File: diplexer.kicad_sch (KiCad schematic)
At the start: 10 parts, among them P25 MMCX-J-P-H-ST-TH1, P26 CONUFL001-SMD-T

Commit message: Change MMCX connectors to right angle
There's not enough room on the board for vertical ones.

Signed-off-by: Corey Minyard <corey@minyard.net>
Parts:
- P25: value MMCX-J-P-H-ST-TH1 -> MMCX-J-P-H-RA-TH1; footprint PacSatDev_misc:COAX4_MMCX-J-P-H-ST-TH1_SAI -> PacSatDev_misc:COAX4_MMCX-J-P-H-RA-TH1_SAI; symbol PACSAT_DEV_misc:MMCX-J-P-H-ST-TH1 -> PACSAT_DEV_misc:MMCX-J-P-H-RA-TH1; now in the parts list
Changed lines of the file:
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@@
 	)
 	(symbol
-		(lib_id "PACSAT_DEV_misc:MMCX-J-P-H-ST-TH1")
+		(lib_id "PACSAT_DEV_misc:MMCX-J-P-H-RA-TH1")
 		(at 133.35 109.22 0)
 		(unit 1)
 		(exclude_from_sim no)
-		(in_bom no)
+		(in_bom yes)
 		(on_board yes)
 		(dnp yes)
@@
 			)
 		)
-		(property "Value" "MMCX-J-P-H-ST-TH1"
+		(property "Value" "MMCX-J-P-H-RA-TH1"
 			(at 133.35 109.22 0)
 			(effects
@@
 			)
 		)
-		(property "Footprint" "PacSatDev_misc:COAX4_MMCX-J-P-H-ST-TH1_SAI"
+		(property "Footprint" "PacSatDev_misc:COAX4_MMCX-J-P-H-RA-TH1_SAI"
 			(at 133.35 109.22 0)
 			(effects
@@
 			)
 		)
-		(property "Datasheet" "MMCX-J-P-H-ST-TH1"
+		(property "Datasheet" "MMCX-J-P-H-RA-TH1"
 			(at 133.35 109.22 0)
 			(effects

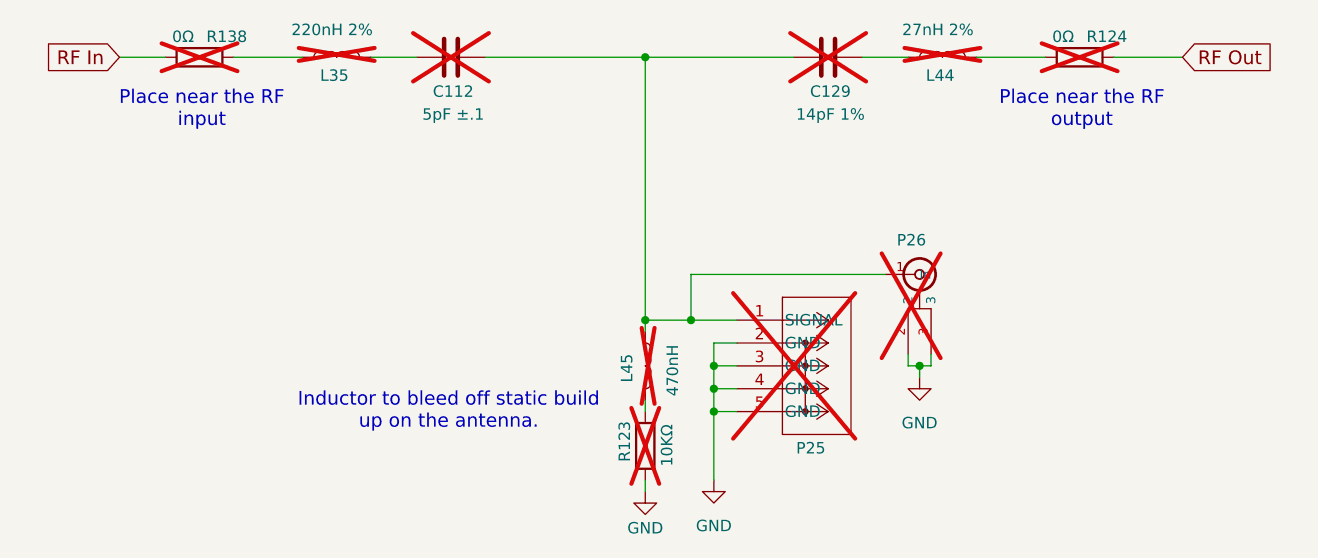
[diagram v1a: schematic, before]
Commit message: Fix issues with the RF connectors
Remove the U.FL connectors P23, P24, and P26 they just weren't going
to work and there's no good place to put them, and where they were was
shorting the MMCX connectors.  Just use the MMCX ones for output.

Move the diplexer MMCX connector to give it more room and get it a
little more out of the way of the transmit connector.

Signed-off-by: Corey Minyard <corey@minyard.net>
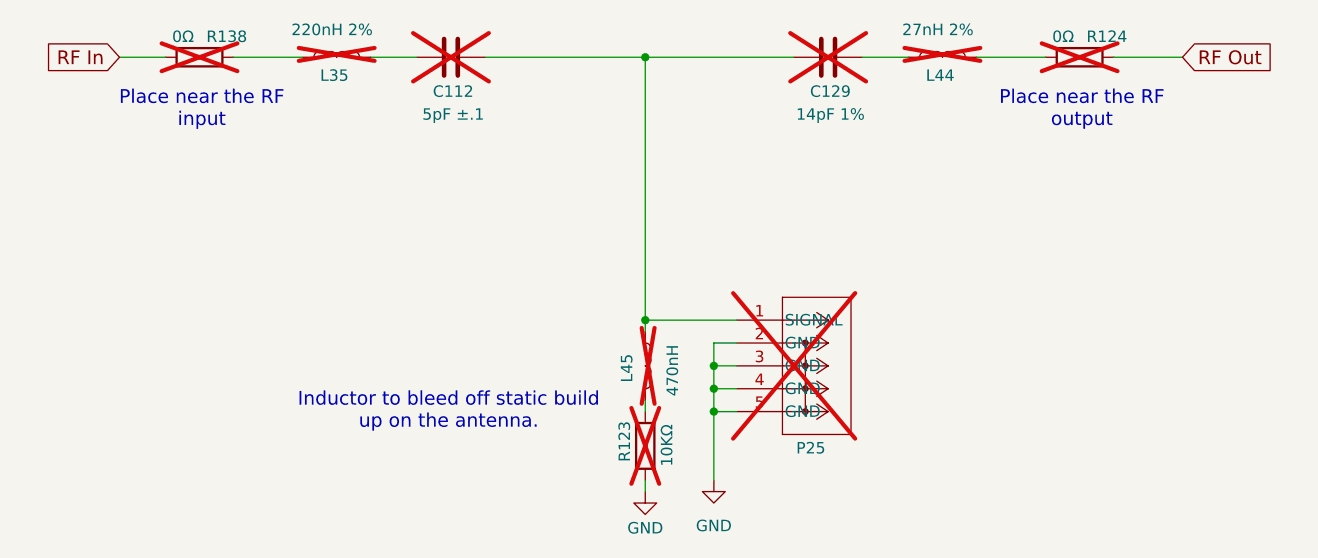
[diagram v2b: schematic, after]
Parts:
- removed P26: CONUFL001-SMD-T, PacSatDev_misc:CONN1_CONUFL_TEC, symbol PACSAT_DEV_misc:U_FL
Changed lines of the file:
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@@
-	)
-	(junction
-		(at 128.27 109.22)
-		(diameter 0)
-		(color 0 0 0 0)
 	)
 	(junction
@@
 	)
 	(junction
-		(at 153.67 114.3)
-		(diameter 0)
-		(color 0 0 0 0)
-	)
-	(junction
 		(at 123.19 80.01)
 		(diameter 0)
@@
 	(wire
 		(pts
-			(xy 153.67 115.57) (xy 153.67 114.3)
-		)
-		(stroke
-			(width 0)
-			(type default)
-		)
-	)
-	(wire
-		(pts
 			(xy 147.32 80.01) (xy 152.4 80.01)
 		)
@@
 	(wire
 		(pts
-			(xy 128.27 104.14) (xy 128.27 109.22)
-		)
-		(stroke
-			(width 0)
-			(type default)
-		)
-	)
-	(wire
-		(pts
 			(xy 133.35 116.84) (xy 130.81 116.84)
 		)
@@
 	(wire
 		(pts
-			(xy 128.27 109.22) (xy 133.35 109.22)
-		)
-		(stroke
-			(width 0)
-			(type default)
-		)
-	)
-	(wire
-		(pts
-			(xy 152.4 113.03) (xy 152.4 114.3)
-		)
-		(stroke
-			(width 0)
-			(type default)
-		)
-	)
-	(wire
-		(pts
-			(xy 154.94 114.3) (xy 153.67 114.3)
+			(xy 123.19 109.22) (xy 133.35 109.22)
 		)
 		(stroke
@@
 	(wire
 		(pts
-			(xy 154.94 113.03) (xy 154.94 114.3)
-		)
-		(stroke
-			(width 0)
-			(type default)
-		)
-	)
-	(wire
-		(pts
 			(xy 92.71 80.01) (xy 97.79 80.01)
 		)
@@
 	(wire
 		(pts
-			(xy 149.86 104.14) (xy 128.27 104.14)
-		)
-		(stroke
-			(width 0)
-			(type default)
-		)
-	)
-	(wire
-		(pts
 			(xy 160.02 80.01) (xy 167.64 80.01)
 		)
@@
 		(pts
 			(xy 130.81 114.3) (xy 130.81 116.84)
-		)
-		(stroke
-			(width 0)
-			(type default)
-		)
-	)
-	(wire
-		(pts
-			(xy 153.67 114.3) (xy 152.4 114.3)
-		)
-		(stroke
-			(width 0)
-			(type default)
-		)
-	)
-	(wire
-		(pts
-			(xy 123.19 109.22) (xy 128.27 109.22)
 		)
 		(stroke
@@
 					(unit 1)
 				)
-			)
-		)
-	)
-	(symbol
-		(lib_id "power:GND")
-		(at 153.67 115.57 0)
-		(mirror y)
-		(unit 1)
-		(exclude_from_sim no)
-		(in_bom yes)
-		(on_board yes)
-		(dnp no)
-		(fields_autoplaced yes)
-		(property "Reference" "#PWR0316"
-			(at 153.67 121.92 0)
-			(effects
-				(font
-					(size 1.27 1.27)
-				)
-				(hide yes)
-			)
-		)
-		(property "Value" "GND"
-			(at 153.67 120.65 0)
-			(effects
-				(font
-					(size 1.27 1.27)
-				)
-			)
-		)
-		(property "Footprint" ""
-			(at 153.67 115.57 0)
-			(effects
-				(font
-					(size 1.27 1.27)
-				)
-				(hide yes)
-			)
-		)
-		(property "Datasheet" ""
-			(at 153.67 115.57 0)
-			(effects
-				(font
-					(size 1.27 1.27)
-				)
-				(hide yes)
-			)
-		)
-		(property "Description" ""
-			(at 153.67 115.57 0)
-			(effects
-				(font
-					(size 1.27 1.27)
-				)
-			)
-		)
-		(pin "1"
-		)
-		(instances
-			(project "PacSat_AFSK"
-				(path "/cc9f42d2-6985-41ac-acab-5ab7b01c5b38/4fa888af-703c-49ed-93bb-d56d2f02c470/38e3adf3-4e99-4cef-9f41-04ced85d0b69"
-					(reference "#PWR0316")
-					(unit 1)
-				)
-			)
-		)
-	)
-	(symbol
-		(lib_id "PACSAT_DEV_misc:U_FL")
-		(at 153.67 104.14 0)
-		(unit 1)
-		(exclude_from_sim no)
-		(in_bom no)
-		(on_board yes)
-		(dnp yes)
-		(property "Reference" "P26"
-			(at 151.13 100.33 0)
-			(effects
-				(font
-					(size 1.27 1.27)
-				)
-				(justify left)
-			)
-		)
-		(property "Value" "CONUFL001-SMD-T"
-			(at 153.67 104.14 0)
-			(effects
-				(font
-					(size 1.27 1.27)
-				)
-				(hide yes)
-			)
-		)
-		(property "Footprint" "PacSatDev_misc:CONN1_CONUFL_TEC"
-			(at 153.67 104.14 0)
-			(effects
-				(font
-					(size 1.27 1.27)
-				)
-				(hide yes)
-			)
-		)
-		(property "Datasheet" ""
-			(at 153.67 104.14 0)
-			(effects
-				(font
-					(size 1.27 1.27)
-				)
-				(hide yes)
-			)
-		)
-		(property "Description" ""
-			(at 153.67 104.14 0)
-			(effects
-				(font
-					(size 1.27 1.27)
-				)
-			)
-		)
-		(pin "1"
-		)
-		(pin "2"
-		)
-		(pin "3"
-		)
-		(instances
-			(project "PacSat_AFSK"
-				(path "/cc9f42d2-6985-41ac-acab-5ab7b01c5b38/4fa888af-703c-49ed-93bb-d56d2f02c470/38e3adf3-4e99-4cef-9f41-04ced85d0b69"
-					(reference "P26")
-					(unit 1)
-				)
